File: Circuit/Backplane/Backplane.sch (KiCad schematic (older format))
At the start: 63 parts

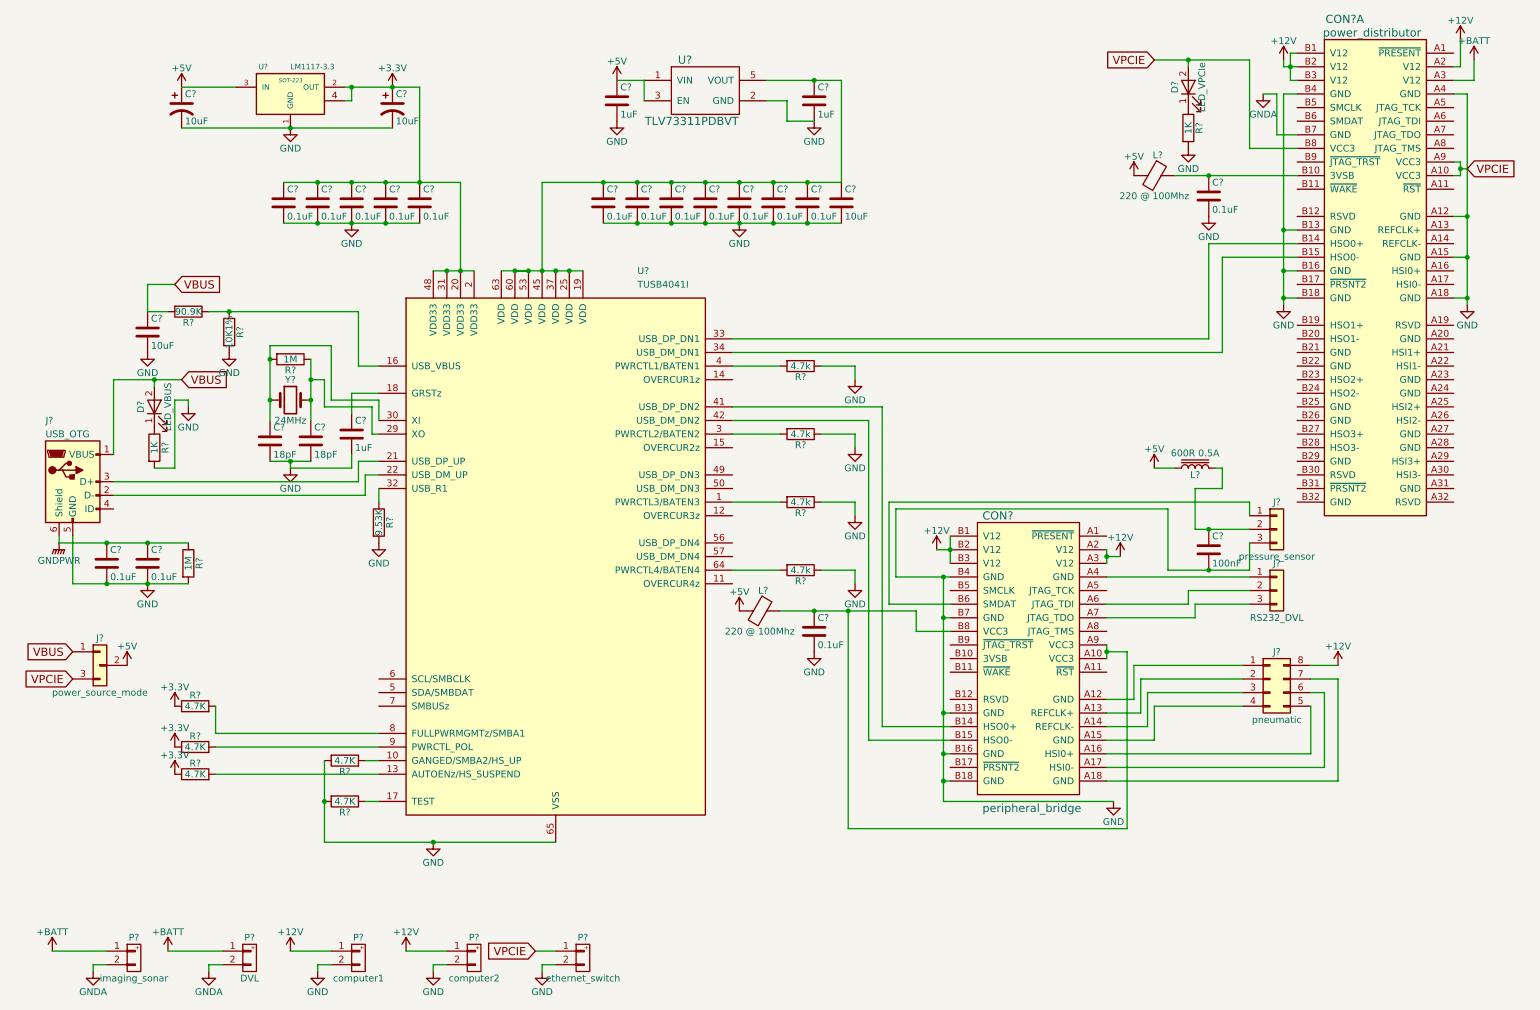
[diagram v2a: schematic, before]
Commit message: redesign LED
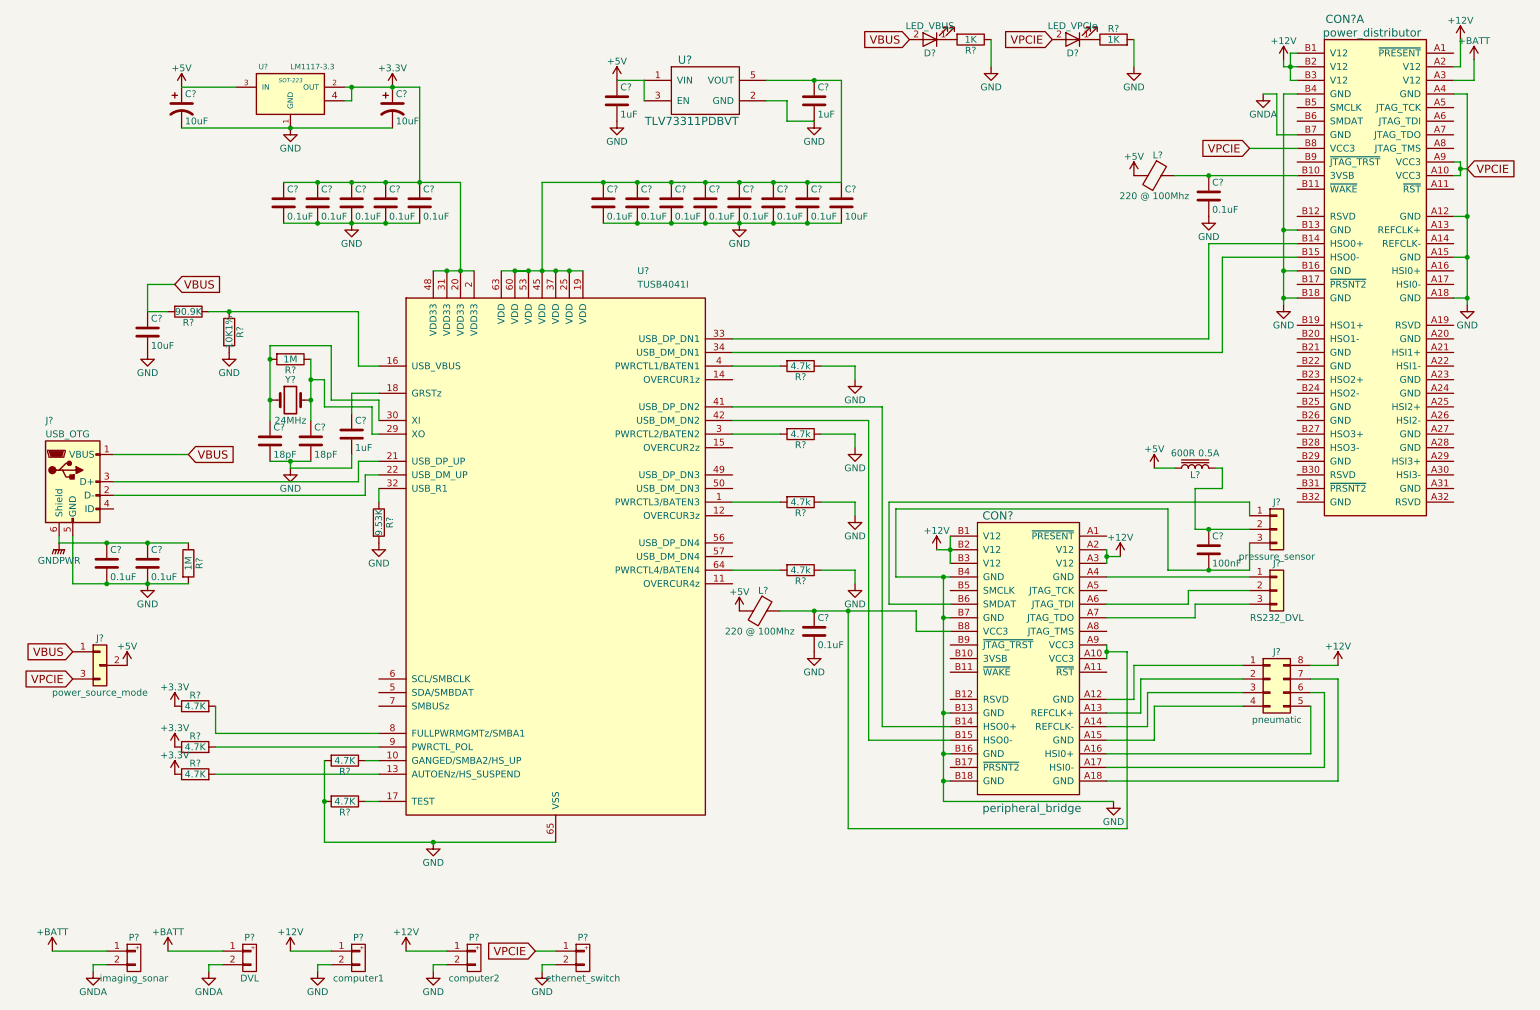
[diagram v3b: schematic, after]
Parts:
- removed D?: LED_VBUS, symbol LED
- removed R?: 1K, symbol R
- added D?: LED_VBUS, symbol LED
- added R?: 1K, symbol R
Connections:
- net GND: now also R?.1
- net VBUS: now also D?.2 (A)
- new net: D?.1 (K), R?.2
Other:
- moved on the sheet: D?, R?
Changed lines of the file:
@@
 	1    0    0    -1
 $EndComp
-Text GLabel 1650 3150 2    60   Input ~ 0
+Text GLabel 1700 3700 2    60   Input ~ 0
 VBUS
 $Comp
@@
 	1    0    0    -1
 $EndComp
-Text GLabel 8800 800  0    60   Input ~ 0
+Text GLabel 9500 1450 0    60   Input ~ 0
 VPCIE
 Text GLabel 11100 1600 2    60   Input ~ 0
@@
 Wire Wire Line
 	9950 5250 10150 5250
-Wire Wire Line
-	8800 800  9500 800
-Wire Wire Line
-	9500 800  9500 1450
-Wire Wire Line
-	9050 800  9050 850
-Connection ~ 9050 800
 $Comp
 L LED D?
 U 1 1 5A628BE7
-P 9050 1000
-F 0 "D?" H 9050 1100 50  0000 C CNN
-F 1 "LED_VPCIe" H 9050 900 50  0000 C CNN
-F 2 "" H 9050 1000 50  0001 C CNN
-F 3 "" H 9050 1000 50  0001 C CNN
-	1    9050 1000
-	0    -1   -1   0
+P 8200 650
+F 0 "D?" H 8200 750 50  0000 C CNN
+F 1 "LED_VPCIe" H 8200 550 50  0000 C CNN
+F 2 "" H 8200 650 50  0001 C CNN
+F 3 "" H 8200 650 50  0001 C CNN
+	1    8200 650
+	-1   0    0    1
 $EndComp
 $Comp
 L R R?
 U 1 1 5A628E18
-P 9050 1300
-F 0 "R?" V 9130 1300 50  0000 C CNN
-F 1 "1K" V 9050 1300 50  0000 C CNN
-F 2 "" V 8980 1300 50  0001 C CNN
-F 3 "" H 9050 1300 50  0001 C CNN
-	1    9050 1300
-	1    0    0    -1
+P 8500 650
+F 0 "R?" V 8580 650 50  0000 C CNN
+F 1 "1K" V 8500 650 50  0000 C CNN
+F 2 "" V 8430 650 50  0001 C CNN
+F 3 "" H 8500 650 50  0001 C CNN
+	1    8500 650
+	0    -1   -1   0
 $EndComp
 $Comp
 L GND #PWR?
 U 1 1 5A628F8E
-P 9050 1450
-F 0 "#PWR?" H 9050 1200 50  0001 C CNN
-F 1 "GND" H 9050 1300 50  0000 C CNN
-F 2 "" H 9050 1450 50  0001 C CNN
-F 3 "" H 9050 1450 50  0001 C CNN
-	1    9050 1450
-	1    0    0    -1
-$EndComp
-Wire Wire Line
-	1150 3700 1150 3150
-Wire Wire Line
-	1150 3150 1650 3150
-Wire Wire Line
-	1450 3150 1450 3200
-Connection ~ 1450 3150
+P 8650 850
+F 0 "#PWR?" H 8650 600 50  0001 C CNN
+F 1 "GND" H 8650 700 50  0000 C CNN
+F 2 "" H 8650 850 50  0001 C CNN
+F 3 "" H 8650 850 50  0001 C CNN
+	1    8650 850
+	1    0    0    -1
+$EndComp
+Wire Wire Line
+	1150 3700 1700 3700
+Text GLabel 7000 650  0    60   Input ~ 0
+VBUS
 $Comp
 L LED D?
-U 1 1 5A62976E
-P 1450 3350
-F 0 "D?" H 1450 3450 50  0000 C CNN
-F 1 "LED_VBUS" H 1450 3250 50  0000 C CNN
-F 2 "" H 1450 3350 50  0001 C CNN
-F 3 "" H 1450 3350 50  0001 C CNN
-	1    1450 3350
-	0    -1   -1   0
+U 1 1 5A63F044
+P 7150 650
+F 0 "D?" H 7150 750 50  0000 C CNN
+F 1 "LED_VBUS" H 7150 550 50  0000 C CNN
+F 2 "" H 7150 650 50  0001 C CNN
+F 3 "" H 7150 650 50  0001 C CNN
+	1    7150 650
+	-1   0    0    1
 $EndComp
 $Comp
 L R R?
-U 1 1 5A629817
-P 1450 3650
-F 0 "R?" V 1530 3650 50  0000 C CNN
-F 1 "1K" V 1450 3650 50  0000 C CNN
-F 2 "" V 1380 3650 50  0001 C CNN
-F 3 "" H 1450 3650 50  0001 C CNN
-	1    1450 3650
-	1    0    0    -1
-$EndComp
-Wire Wire Line
-	1450 3800 1600 3800
-Wire Wire Line
-	1600 3800 1600 3300
-Wire Wire Line
-	1600 3300 1700 3300
-Wire Wire Line
-	1700 3300 1700 3350
-$Comp
-L GND #PWR?
-U 1 1 5A629A10
-P 1700 3350
-F 0 "#PWR?" H 1700 3100 50  0001 C CNN
-F 1 "GND" H 1700 3200 50  0000 C CNN
-F 2 "" H 1700 3350 50  0001 C CNN
-F 3 "" H 1700 3350 50  0001 C CNN
-	1    1700 3350
-	1    0    0    -1
-$EndComp
+U 1 1 5A63F04A
+P 7450 650
+F 0 "R?" V 7530 650 50  0000 C CNN
+F 1 "1K" V 7450 650 50  0000 C CNN
+F 2 "" V 7380 650 50  0001 C CNN
+F 3 "" H 7450 650 50  0001 C CNN
+	1    7450 650
+	0    1    1    0
+$EndComp
+Wire Wire Line
+	7600 650  7600 850
+$Comp
+L GND #PWR?
+U 1 1 5A63F094
+P 7600 850
+F 0 "#PWR?" H 7600 600 50  0001 C CNN
+F 1 "GND" H 7600 700 50  0000 C CNN
+F 2 "" H 7600 850 50  0001 C CNN
+F 3 "" H 7600 850 50  0001 C CNN
+	1    7600 850
+	1    0    0    -1
+$EndComp
+Text GLabel 8050 650  0    60   Input ~ 0
+VPCIE
+Wire Wire Line
+	8650 650  8650 850
 $EndSCHEMATC

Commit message: AddGeneral
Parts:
- added J?: Conn_Jumper, symbol Conn_Jumper
- added P?: General, symbol XT30
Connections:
- net +12V: now also J?.1 (Pin_1)
- net GND: now also J?.3 (Pin_3), P?.2 (P2)
- new net: J?.2 (Pin_2), P?.1 (P1)
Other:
- moved on the sheet: C?, R?, Y?
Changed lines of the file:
@@
 L R R?
 U 1 1 5A64A969
-P 2450 3000
-F 0 "R?" V 2530 3000 50  0000 C CNN
-F 1 "1M" V 2450 3000 50  0000 C CNN
-F 2 "" V 2380 3000 50  0001 C CNN
-F 3 "" H 2450 3000 50  0001 C CNN
-	1    2450 3000
+P 2450 2900
+F 0 "R?" V 2530 2900 50  0000 C CNN
+F 1 "1M" V 2450 2900 50  0000 C CNN
+F 2 "" V 2380 2900 50  0001 C CNN
+F 3 "" H 2450 2900 50  0001 C CNN
+	1    2450 2900
 	0    1    1    0
 $EndComp
@@
 L Crystal Y?
 U 1 1 5A64AB53
-P 2450 3300
-F 0 "Y?" H 2450 3450 50  0000 C CNN
-F 1 "24MHz" H 2450 3150 50  0000 C CNN
-F 2 "" H 2450 3300 50  0001 C CNN
-F 3 "" H 2450 3300 50  0001 C CNN
-	1    2450 3300
+P 2450 3200
+F 0 "Y?" H 2450 3350 50  0000 C CNN
+F 1 "24MHz" H 2450 3050 50  0000 C CNN
+F 2 "" H 2450 3200 50  0001 C CNN
+F 3 "" H 2450 3200 50  0001 C CNN
+	1    2450 3200
 	1    0    0    -1
 $EndComp
@@
 L C C?
 U 1 1 5A64AFC4
-P 2300 3600
-F 0 "C?" H 2325 3700 50  0000 L CNN
-F 1 "18pF" H 2325 3500 50  0000 L CNN
-F 2 "" H 2338 3450 50  0001 C CNN
-F 3 "" H 2300 3600 50  0001 C CNN
-	1    2300 3600
+P 2300 3500
+F 0 "C?" H 2325 3600 50  0000 L CNN
+F 1 "18pF" H 2325 3400 50  0000 L CNN
+F 2 "" H 2338 3350 50  0001 C CNN
+F 3 "" H 2300 3500 50  0001 C CNN
+	1    2300 3500
 	1    0    0    -1
 $EndComp
@@
 L C C?
 U 1 1 5A64B075
-P 2600 3600
-F 0 "C?" H 2625 3700 50  0000 L CNN
-F 1 "18pF" H 2625 3500 50  0000 L CNN
-F 2 "" H 2638 3450 50  0001 C CNN
-F 3 "" H 2600 3600 50  0001 C CNN
-	1    2600 3600
+P 2600 3500
+F 0 "C?" H 2625 3600 50  0000 L CNN
+F 1 "18pF" H 2625 3400 50  0000 L CNN
+F 2 "" H 2638 3350 50  0001 C CNN
+F 3 "" H 2600 3500 50  0001 C CNN
+	1    2600 3500
 	1    0    0    -1
 $EndComp
@@
 L GND #PWR?
 U 1 1 5A64B57C
-P 2450 3800
-F 0 "#PWR?" H 2450 3550 50  0001 C CNN
-F 1 "GND" H 2450 3650 50  0000 C CNN
-F 2 "" H 2450 3800 50  0001 C CNN
-F 3 "" H 2450 3800 50  0001 C CNN
-	1    2450 3800
+P 2450 3700
+F 0 "#PWR?" H 2450 3450 50  0001 C CNN
+F 1 "GND" H 2450 3550 50  0000 C CNN
+F 2 "" H 2450 3700 50  0001 C CNN
+F 3 "" H 2450 3700 50  0001 C CNN
+	1    2450 3700
 	1    0    0    -1
 $EndComp
@@
 	1    0    0    -1
 $EndComp
+$Comp
+L LED D?
+U 1 1 5A628BE7
+P 8200 650
+F 0 "D?" H 8200 750 50  0000 C CNN
+F 1 "LED_VPCIe" H 8200 550 50  0000 C CNN
+F 2 "" H 8200 650 50  0001 C CNN
+F 3 "" H 8200 650 50  0001 C CNN
+	1    8200 650
+	-1   0    0    1
+$EndComp
+$Comp
+L R R?
+U 1 1 5A628E18
+P 8500 650
+F 0 "R?" V 8580 650 50  0000 C CNN
+F 1 "1K" V 8500 650 50  0000 C CNN
+F 2 "" V 8430 650 50  0001 C CNN
+F 3 "" H 8500 650 50  0001 C CNN
+	1    8500 650
+	0    -1   -1   0
+$EndComp
+$Comp
+L GND #PWR?
+U 1 1 5A628F8E
+P 8650 850
+F 0 "#PWR?" H 8650 600 50  0001 C CNN
+F 1 "GND" H 8650 700 50  0000 C CNN
+F 2 "" H 8650 850 50  0001 C CNN
+F 3 "" H 8650 850 50  0001 C CNN
+	1    8650 850
+	1    0    0    -1
+$EndComp
+Text GLabel 7000 650  0    60   Input ~ 0
+VBUS
+$Comp
+L LED D?
+U 1 1 5A63F044
+P 7150 650
+F 0 "D?" H 7150 750 50  0000 C CNN
+F 1 "LED_VBUS" H 7150 550 50  0000 C CNN
+F 2 "" H 7150 650 50  0001 C CNN
+F 3 "" H 7150 650 50  0001 C CNN
+	1    7150 650
+	-1   0    0    1
+$EndComp
+$Comp
+L R R?
+U 1 1 5A63F04A
+P 7450 650
+F 0 "R?" V 7530 650 50  0000 C CNN
+F 1 "1K" V 7450 650 50  0000 C CNN
+F 2 "" V 7380 650 50  0001 C CNN
+F 3 "" H 7450 650 50  0001 C CNN
+	1    7450 650
+	0    1    1    0
+$EndComp
+$Comp
+L GND #PWR?
+U 1 1 5A63F094
+P 7600 850
+F 0 "#PWR?" H 7600 600 50  0001 C CNN
+F 1 "GND" H 7600 700 50  0000 C CNN
+F 2 "" H 7600 850 50  0001 C CNN
+F 3 "" H 7600 850 50  0001 C CNN
+	1    7600 850
+	1    0    0    -1
+$EndComp
+Text GLabel 8050 650  0    60   Input ~ 0
+VPCIE
+$Comp
+L GND #PWR?
+U 1 1 5A65DB26
+P 6000 7500
+F 0 "#PWR?" H 6000 7250 50  0001 C CNN
+F 1 "GND" H 6000 7350 50  0000 C CNN
+F 2 "" H 6000 7500 50  0001 C CNN
+F 3 "" H 6000 7500 50  0001 C CNN
+	1    6000 7500
+	1    0    0    -1
+$EndComp
+$Comp
+L XT30 P?
+U 1 1 5A65DB20
+P 6300 7400
+F 0 "P?" H 6300 7550 50  0000 C CNN
+F 1 "General" H 6300 7250 50  0000 C CNN
+F 2 "" H 6300 7400 60  0000 C CNN
+F 3 "" H 6300 7400 60  0000 C CNN
+	1    6300 7400
+	1    0    0    -1
+$EndComp
+$Comp
+L Conn_Jumper J?
+U 1 1 5A65DF87
+P 5450 7350
+F 0 "J?" H 5450 7550 50  0000 C CNN
+F 1 "Conn_Jumper" H 5450 7150 50  0000 C CNN
+F 2 "" H 5500 7350 50  0001 C CNN
+F 3 "" H 5500 7350 50  0001 C CNN
+	1    5450 7350
+	1    0    0    -1
+$EndComp
+Wire Wire Line
+	5050 7250 5050 7200
+Wire Wire Line
+	5250 7250 5050 7250
+Wire Wire Line
+	5650 7350 6100 7350
+Wire Wire Line
+	6100 7450 6000 7450
+Wire Wire Line
+	6000 7450 6000 7500
 Wire Wire Line
 	6800 5700 7300 5700
@@
 Connection ~ 2650 2000
 Wire Wire Line
-	4300 1700 6500 1700
+	6500 1700 4300 1700
 Connection ~ 5000 1700
 Connection ~ 5250 1700
@@
 Connection ~ 3500 6550
 Wire Wire Line
-	8450 5150 8600 5150
+	8600 5150 8450 5150
 Connection ~ 8450 5150
 Wire Wire Line
@@
 	3100 3300 2750 3300
 Wire Wire Line
-	2750 3300 2750 2900
-Wire Wire Line
-	2750 2900 2300 2900
-Wire Wire Line
-	2300 2900 2300 3450
-Wire Wire Line
-	2600 3000 2600 3450
-Connection ~ 2300 3000
-Wire Wire Line
-	3100 3550 3050 3550
-Wire Wire Line
-	3050 3550 3050 3350
-Wire Wire Line
-	3050 3350 2700 3350
-Wire Wire Line
-	2700 3350 2700 3150
-Wire Wire Line
-	2700 3150 2600 3150
-Connection ~ 2600 3150
-Connection ~ 2600 3300
-Connection ~ 2300 3300
-Wire Wire Line
-	2300 3750 2600 3750
-Wire Wire Line
-	2450 3750 2450 3800
-Connection ~ 2450 3750
+	2750 3300 2750 2800
+Wire Wire Line
+	2750 2800 2300 2800
+Wire Wire Line
+	2300 2800 2300 3350
+Wire Wire Line
+	2600 2900 2600 3350
+Connection ~ 2300 2900
+Wire Wire Line
+	3050 3550 3100 3550
+Wire Wire Line
+	3050 3350 3050 3550
+Wire Wire Line
+	2700 3350 3050 3350
+Connection ~ 2600 3200
+Connection ~ 2300 3200
+Wire Wire Line
+	2300 3650 2600 3650
+Wire Wire Line
+	2450 3650 2450 3700
+Connection ~ 2450 3650
 Wire Wire Line
 	3100 3250 2900 3250
@@
 	2900 3250 2900 3400
 Wire Wire Line
-	2900 3700 2900 3800
-Wire Wire Line
-	2900 3800 2450 3800
+	2900 3800 2900 3700
 Wire Wire Line
 	2950 3900 2950 3750
@@
 Wire Wire Line
 	9950 5250 10150 5250
-$Comp
-L LED D?
-U 1 1 5A628BE7
-P 8200 650
-F 0 "D?" H 8200 750 50  0000 C CNN
-F 1 "LED_VPCIe" H 8200 550 50  0000 C CNN
-F 2 "" H 8200 650 50  0001 C CNN
-F 3 "" H 8200 650 50  0001 C CNN
-	1    8200 650
-	-1   0    0    1
-$EndComp
-$Comp
-L R R?
-U 1 1 5A628E18
-P 8500 650
-F 0 "R?" V 8580 650 50  0000 C CNN
-F 1 "1K" V 8500 650 50  0000 C CNN
-F 2 "" V 8430 650 50  0001 C CNN
-F 3 "" H 8500 650 50  0001 C CNN
-	1    8500 650
-	0    -1   -1   0
-$EndComp
-$Comp
-L GND #PWR?
-U 1 1 5A628F8E
-P 8650 850
-F 0 "#PWR?" H 8650 600 50  0001 C CNN
-F 1 "GND" H 8650 700 50  0000 C CNN
-F 2 "" H 8650 850 50  0001 C CNN
-F 3 "" H 8650 850 50  0001 C CNN
-	1    8650 850
-	1    0    0    -1
-$EndComp
 Wire Wire Line
 	1150 3700 1700 3700
-Text GLabel 7000 650  0    60   Input ~ 0
-VBUS
-$Comp
-L LED D?
-U 1 1 5A63F044
-P 7150 650
-F 0 "D?" H 7150 750 50  0000 C CNN
-F 1 "LED_VBUS" H 7150 550 50  0000 C CNN
-F 2 "" H 7150 650 50  0001 C CNN
-F 3 "" H 7150 650 50  0001 C CNN
-	1    7150 650
-	-1   0    0    1
-$EndComp
-$Comp
-L R R?
-U 1 1 5A63F04A
-P 7450 650
-F 0 "R?" V 7530 650 50  0000 C CNN
-F 1 "1K" V 7450 650 50  0000 C CNN
-F 2 "" V 7380 650 50  0001 C CNN
-F 3 "" H 7450 650 50  0001 C CNN
-	1    7450 650
-	0    1    1    0
-$EndComp
 Wire Wire Line
 	7600 650  7600 850
-$Comp
-L GND #PWR?
-U 1 1 5A63F094
-P 7600 850
-F 0 "#PWR?" H 7600 600 50  0001 C CNN
-F 1 "GND" H 7600 700 50  0000 C CNN
-F 2 "" H 7600 850 50  0001 C CNN
-F 3 "" H 7600 850 50  0001 C CNN
-	1    7600 850
-	1    0    0    -1
-$EndComp
-Text GLabel 8050 650  0    60   Input ~ 0
+Wire Wire Line
+	8650 650  8650 850
+Wire Wire Line
+	2600 3200 2700 3200
+Wire Wire Line
+	2700 3200 2700 3350
+Wire Wire Line
+	2600 3650 2600 3800
+Wire Wire Line
+	2600 3800 2900 3800
+$Comp
+L +12V #PWR?
+U 1 1 5A65EB25
+P 5050 7200
+F 0 "#PWR?" H 5050 7050 50  0001 C CNN
+F 1 "+12V" H 5050 7340 50  0000 C CNN
+F 2 "" H 5050 7200 50  0001 C CNN
+F 3 "" H 5050 7200 50  0001 C CNN
+	1    5050 7200
+	1    0    0    -1
+$EndComp
+Text GLabel 5250 7450 0    60   Input ~ 0
 VPCIE
-Wire Wire Line
-	8650 650  8650 850
 $EndSCHEMATC

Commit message: ChangeGeneralocation
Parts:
- J?: value Conn_Jumper -> General_Power_Source
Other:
- moved on the sheet: J?, P?
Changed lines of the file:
@@
 L Conn_Jumper J?
 U 1 1 5A5DEBD0
-P 1050 5250
-F 0 "J?" H 1050 5450 50  0000 C CNN
-F 1 "power_source_mode" H 1050 5050 50  0000 C CNN
-F 2 "" H 1100 5250 50  0001 C CNN
-F 3 "" H 1100 5250 50  0001 C CNN
-	1    1050 5250
-	1    0    0    -1
-$EndComp
-Text GLabel 850  5150 0    60   Input ~ 0
+P 1050 5700
+F 0 "J?" H 1050 5900 50  0000 C CNN
+F 1 "power_source_mode" H 1050 5500 50  0000 C CNN
+F 2 "" H 1100 5700 50  0001 C CNN
+F 3 "" H 1100 5700 50  0001 C CNN
+	1    1050 5700
+	1    0    0    -1
+$EndComp
+Text GLabel 850  5600 0    60   Input ~ 0
 VBUS
-Text GLabel 850  5350 0    60   Input ~ 0
+Text GLabel 850  5800 0    60   Input ~ 0
 VPCIE
 $Comp
@@
 L +5V #PWR?
 U 1 1 5A60F609
-P 1250 5250
-F 0 "#PWR?" H 1250 5100 50  0001 C CNN
-F 1 "+5V" H 1250 5390 50  0000 C CNN
-F 2 "" H 1250 5250 50  0001 C CNN
-F 3 "" H 1250 5250 50  0001 C CNN
-	1    1250 5250
+P 1250 5700
+F 0 "#PWR?" H 1250 5550 50  0001 C CNN
+F 1 "+5V" H 1250 5840 50  0000 C CNN
+F 2 "" H 1250 5700 50  0001 C CNN
+F 3 "" H 1250 5700 50  0001 C CNN
+	1    1250 5700
 	1    0    0    -1
 $EndComp
@@
 L GND #PWR?
 U 1 1 5A65DB26
-P 6000 7500
-F 0 "#PWR?" H 6000 7250 50  0001 C CNN
-F 1 "GND" H 6000 7350 50  0000 C CNN
-F 2 "" H 6000 7500 50  0001 C CNN
-F 3 "" H 6000 7500 50  0001 C CNN
-	1    6000 7500
+P 1850 6650
+F 0 "#PWR?" H 1850 6400 50  0001 C CNN
+F 1 "GND" H 1850 6500 50  0000 C CNN
+F 2 "" H 1850 6650 50  0001 C CNN
+F 3 "" H 1850 6650 50  0001 C CNN
+	1    1850 6650
 	1    0    0    -1
 $EndComp
@@
 L XT30 P?
 U 1 1 5A65DB20
-P 6300 7400
-F 0 "P?" H 6300 7550 50  0000 C CNN
-F 1 "General" H 6300 7250 50  0000 C CNN
-F 2 "" H 6300 7400 60  0000 C CNN
-F 3 "" H 6300 7400 60  0000 C CNN
-	1    6300 7400
+P 2150 6550
+F 0 "P?" H 2150 6700 50  0000 C CNN
+F 1 "General" H 2150 6400 50  0000 C CNN
+F 2 "" H 2150 6550 60  0000 C CNN
+F 3 "" H 2150 6550 60  0000 C CNN
+	1    2150 6550
 	1    0    0    -1
 $EndComp
@@
 L Conn_Jumper J?
 U 1 1 5A65DF87
-P 5450 7350
-F 0 "J?" H 5450 7550 50  0000 C CNN
-F 1 "Conn_Jumper" H 5450 7150 50  0000 C CNN
-F 2 "" H 5500 7350 50  0001 C CNN
-F 3 "" H 5500 7350 50  0001 C CNN
-	1    5450 7350
-	1    0    0    -1
-$EndComp
-Wire Wire Line
-	5050 7250 5050 7200
-Wire Wire Line
-	5250 7250 5050 7250
-Wire Wire Line
-	5650 7350 6100 7350
-Wire Wire Line
-	6100 7450 6000 7450
-Wire Wire Line
-	6000 7450 6000 7500
+P 1050 6500
+F 0 "J?" H 1050 6700 50  0000 C CNN
+F 1 "General_Power_Source" H 1050 6300 50  0000 C CNN
+F 2 "" H 1100 6500 50  0001 C CNN
+F 3 "" H 1100 6500 50  0001 C CNN
+	1    1050 6500
+	1    0    0    -1
+$EndComp
+Wire Wire Line
+	650  6400 650  6350
+Wire Wire Line
+	850  6400 650  6400
+Wire Wire Line
+	1250 6500 1950 6500
+Wire Wire Line
+	1950 6600 1850 6600
+Wire Wire Line
+	1850 6600 1850 6650
 Wire Wire Line
 	6800 5700 7300 5700
@@
 L +12V #PWR?
 U 1 1 5A65EB25
-P 5050 7200
-F 0 "#PWR?" H 5050 7050 50  0001 C CNN
-F 1 "+12V" H 5050 7340 50  0000 C CNN
-F 2 "" H 5050 7200 50  0001 C CNN
-F 3 "" H 5050 7200 50  0001 C CNN
-	1    5050 7200
-	1    0    0    -1
-$EndComp
-Text GLabel 5250 7450 0    60   Input ~ 0
+P 650 6350
+F 0 "#PWR?" H 650 6200 50  0001 C CNN
+F 1 "+12V" H 650 6490 50  0000 C CNN
+F 2 "" H 650 6350 50  0001 C CNN
+F 3 "" H 650 6350 50  0001 C CNN
+	1    650  6350
+	1    0    0    -1
+$EndComp
+Text GLabel 850  6600 0    60   Input ~ 0
 VPCIE
 $EndSCHEMATC
